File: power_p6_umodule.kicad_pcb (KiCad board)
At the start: 4 copper layers, 44.8 x 41.5 mm, 25 parts, among them J1 LSHM-140-04.0-L-DV-A-N-K-TR, U1 LTM4653EY

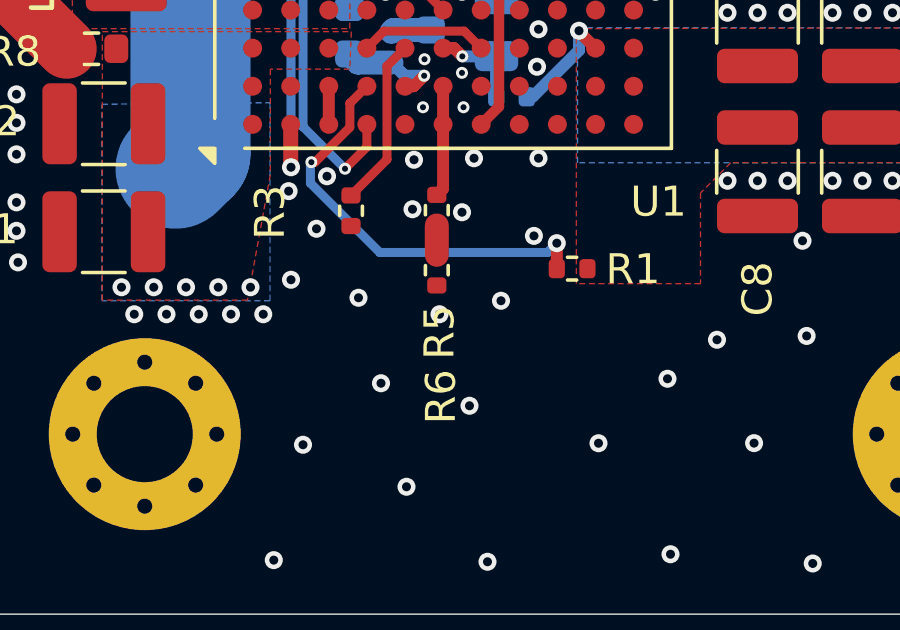
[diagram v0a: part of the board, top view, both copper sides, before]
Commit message: update set resistor to thin film.
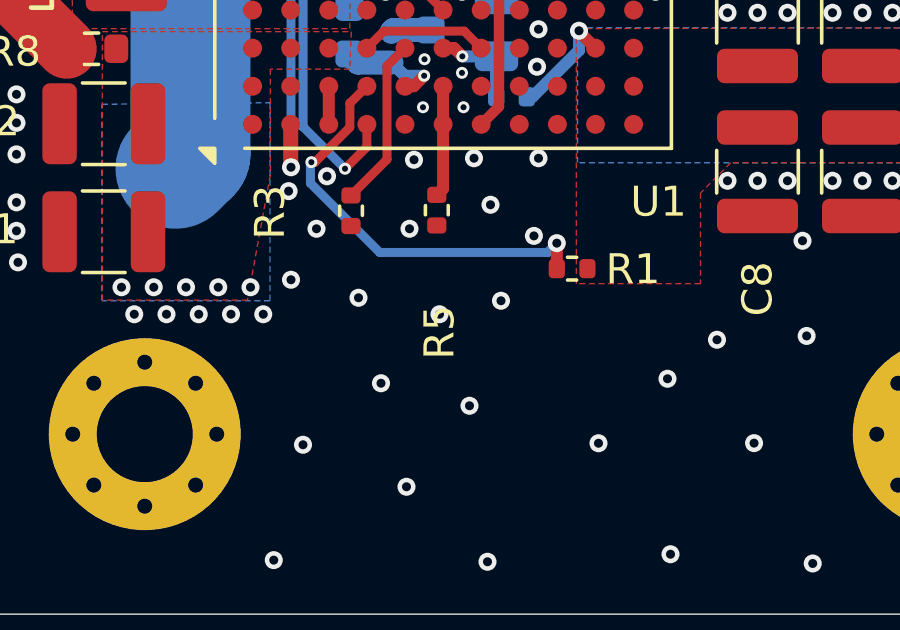
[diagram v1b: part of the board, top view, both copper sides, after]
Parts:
- removed R6: 2k, Resistor_SMD:R_0402_1005Metric
- R5: value 118k -> 120k
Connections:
- R5 pad 2: /iset2 -> GND
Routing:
- net /iset2: track 0.98 -> 0.00 mm
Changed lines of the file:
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@@
 	(net 43 "unconnected-(U1-NC-PadK6)")
 	(net 44 "unconnected-(U1-NC-PadC7)")
-	(net 45 "/iset2")
-	(net 46 "/iset")
-	(net 47 "/vosns")
-	(net 48 "/ser")
-	(net 49 "/cf1")
-	(footprint "Resistor_SMD:R_0402_1005Metric"
-		(layer "F.Cu")
-		(at 121.51 73.88 -90)
-		(descr "Resistor SMD 0402 (1005 Metric), square (rectangular) end terminal, IPC-7351 nominal, (Body size source: IPC-SM-782 page 72, https://www.pcb-3d.com/wordpress/wp-content/uploads/ipc-sm-782a_amendment_1_and_2.pdf), generated with kicad-footprint-generator")
-		(tags "resistor")
-		(property "Reference" "R6"
-			(at 4.22 -0.14 90)
-			(layer "F.SilkS")
-			(effects
-				(font
-					(size 1 1)
-					(thickness 0.15)
-				)
-			)
-		)
-		(property "Value" "2k"
-			(at 0 1.17 90)
-			(layer "F.Fab")
-			(effects
-				(font
-					(size 1 1)
-					(thickness 0.15)
-				)
-			)
-		)
-		(property "Datasheet" "~"
-			(at 0 0 90)
-			(layer "F.Fab")
-			(hide yes)
-			(effects
-				(font
-					(size 1.27 1.27)
-					(thickness 0.15)
-				)
-			)
-		)
-		(property "Description" "2 kOhms ±1% 0.1W, 1/10W Chip Resistor 0402 (1005 Metric) Automotive AEC-Q200 Thick Film"
-			(at 0 0 90)
-			(layer "F.Fab")
-			(hide yes)
-			(effects
-				(font
-					(size 1.27 1.27)
-					(thickness 0.15)
-				)
-			)
-		)
-		(property "M" "Vishay"
-			(at 0 0 270)
-			(unlocked yes)
-			(layer "F.Fab")
-			(hide yes)
-			(effects
-				(font
-					(size 1 1)
-					(thickness 0.15)
-				)
-			)
-		)
-		(property "MPN" "CRCW04022K00FKED"
-			(at 0 0 270)
-			(unlocked yes)
-			(layer "F.Fab")
-			(hide yes)
-			(effects
-				(font
-					(size 1 1)
-					(thickness 0.15)
-				)
-			)
-		)
-		(property ki_fp_filters "R_*")
-		(sheetname "/")
-		(sheetfile "power_p6_umodule.kicad_sch")
-		(attr smd)
-		(fp_line
-			(start -0.153641 0.38)
-			(end 0.153641 0.38)
-			(stroke
-				(width 0.12)
-				(type solid)
-			)
-			(layer "F.SilkS")
-		)
-		(fp_line
-			(start -0.153641 -0.38)
-			(end 0.153641 -0.38)
-			(stroke
-				(width 0.12)
-				(type solid)
-			)
-			(layer "F.SilkS")
-		)
-		(fp_rect
-			(start -0.93 -0.47)
-			(end 0.93 0.47)
-			(stroke
-				(width 0.05)
-				(type solid)
-			)
-			(fill no)
-			(layer "F.CrtYd")
-		)
-		(fp_rect
-			(start -0.525 -0.27)
-			(end 0.525 0.27)
-			(stroke
-				(width 0.1)
-				(type solid)
-			)
-			(fill no)
-			(layer "F.Fab")
-		)
-		(fp_text user "${REFERENCE}"
-			(at 0 0 90)
-			(layer "F.Fab")
-			(effects
-				(font
-					(size 0.26 0.26)
-					(thickness 0.04)
-				)
-			)
-		)
-		(pad "1" smd roundrect
-			(at -0.51 0 270)
-			(size 0.54 0.64)
-			(layers "F.Cu" "F.Mask" "F.Paste")
-			(roundrect_rratio 0.25)
-			(net 45 "/iset2")
-			(pintype "passive")
-		)
-		(pad "2" smd roundrect
-			(at 0.51 0 270)
-			(size 0.54 0.64)
-			(layers "F.Cu" "F.Mask" "F.Paste")
-			(roundrect_rratio 0.25)
-			(net 2 "GND")
-			(pintype "passive")
-		)
-		(embedded_fonts no)
-		(model "${KICAD9_3DMODEL_DIR}/Resistor_SMD.3dshapes/R_0402_1005Metric.step"
-			(offset
-				(xyz 0 0 0)
-			)
-			(scale
-				(xyz 1 1 1)
-			)
-			(rotate
-				(xyz 0 0 0)
-			)
-		)
-	)
+	(net 45 "/iset")
+	(net 46 "/vosns")
+	(net 47 "/ser")
+	(net 48 "/cf1")
 	(footprint "Capacitor_Tantalum_SMD:CP_EIA-7343-20_Kemet-V"
 		(layer "F.Cu")
@@
 			(layers "F.Cu" "F.Mask" "F.Paste")
 			(roundrect_rratio 0.120773)
-			(net 48 "/ser")
+			(net 47 "/ser")
 			(pintype "passive")
 		)
@@
 			(property pad_prop_bga)
 			(layers "F.Cu" "F.Mask" "F.Paste")
-			(net 46 "/iset")
+			(net 45 "/iset")
 			(pinfunction "ISETB")
 			(pintype "unspecified")
@@
 			(property pad_prop_bga)
 			(layers "F.Cu" "F.Mask" "F.Paste")
-			(net 46 "/iset")
+			(net 45 "/iset")
 			(pinfunction "ISETA")
 			(pintype "unspecified")
@@
 			(property pad_prop_bga)
 			(layers "F.Cu" "F.Mask" "F.Paste")
-			(net 47 "/vosns")
+			(net 46 "/vosns")
 			(pinfunction "VOSNS")
 			(pintype "unspecified")
@@
 			(size 0.5 0.5)
 			(layers "F.Cu")
-			(net 47 "/vosns")
+			(net 46 "/vosns")
 			(pinfunction "1")
 			(pintype "passive")
@@
 			(size 2.499995 2.560396)
 			(layers "F.Cu" "F.Mask" "F.Paste")
-			(net 49 "/cf1")
+			(net 48 "/cf1")
 			(pintype "passive")
 		)
@@
 			(layers "F.Cu" "F.Mask" "F.Paste")
 			(roundrect_rratio 0.25)
-			(net 49 "/cf1")
+			(net 48 "/cf1")
 			(pintype "passive")
 		)
@@
 			)
 		)
-		(property "Value" "118k"
+		(property "Value" "120k"
 			(at 0 1.17 90)
 			(layer "F.Fab")
@@
 			)
 		)
-		(property "Description" "118 kOhms ±1% 0.1W, 1/10W Chip Resistor 0402 (1005 Metric) Automotive AEC-Q200 Thick Film"
+		(property "Description" "120 kOhms ±1% 0.063W, 1/16W Chip Resistor 0402 (1005 Metric) Anti-Sulfur Thin Film"
 			(at 0 0 90)
 			(layer "F.Fab")
@@
 			)
 		)
-		(property "M" "Vishay"
+		(property "M" "Yageo"
 			(at 0 0 270)
 			(unlocked yes)
@@
 			)
 		)
-		(property "MPN" "CRCW0402118KFKED"
+		(property "MPN" "MCS04020C1203FE000"
 			(at 0 0 270)
 			(unlocked yes)
@@
 			(layers "F.Cu" "F.Mask" "F.Paste")
 			(roundrect_rratio 0.25)
-			(net 46 "/iset")
+			(net 45 "/iset")
 			(pintype "passive")
 		)
@@
 			(layers "F.Cu" "F.Mask" "F.Paste")
 			(roundrect_rratio 0.25)
-			(net 45 "/iset2")
+			(net 2 "GND")
 			(pintype "passive")
 		)
@@
 			(layers "F.Cu" "F.Mask" "F.Paste")
 			(roundrect_rratio 0.25)
-			(net 48 "/ser")
+			(net 47 "/ser")
 			(pintype "passive")
 		)
@@
 	)
 	(via
-		(at 122.35 71.95)
+		(at 123.3 71.7)
 		(size 0.6)
 		(drill 0.3)
@@
 	)
 	(via
-		(at 120.7 71.85)
+		(at 120.6 72.5)
 		(size 0.6)
 		(drill 0.3)
@@
 	)
 	(segment
-		(start 121.51 72.39)
-		(end 121.51 73.37)
-		(width 0.8)
-		(layer "F.Cu")
-		(net 45)
-	)
-	(segment
 		(start 121.72 71.16)
 		(end 121.51 71.37)
 		(width 0.4)
 		(layer "F.Cu")
-		(net 46)
+		(net 45)
 	)
 	(segment
@@
 		(width 0.4)
 		(layer "F.Cu")
-		(net 46)
+		(net 45)
 	)
 	(segment
@@
 		(width 0.4)
 		(layer "F.Cu")
-		(net 46)
+		(net 45)
 	)
 	(segment
@@
 		(width 0.35)
 		(layer "F.Cu")
-		(net 47)
+		(net 46)
 	)
 	(segment
@@
 		(width 0.35)
 		(layer "F.Cu")
-		(net 47)
+		(net 46)
 	)
 	(segment
@@
 		(width 0.35)
 		(layer "F.Cu")
-		(net 47)
+		(net 46)
 	)
 	(segment
@@
 		(width 0.35)
 		(layer "F.Cu")
-		(net 47)
+		(net 46)
 	)
 	(segment
@@
 		(width 2)
 		(layer "F.Cu")
-		(net 48)
+		(net 47)
 	)
 	(segment
@@
 		(width 2)
 		(layer "F.Cu")
-		(net 48)
+		(net 47)
 	)
 	(segment
@@
 		(width 2)
 		(layer "F.Cu")
-		(net 49)
+		(net 48)
 	)
 	(segment
@@
 		(width 2)
 		(layer "F.Cu")
-		(net 49)
+		(net 48)
 	)
 	(zone
